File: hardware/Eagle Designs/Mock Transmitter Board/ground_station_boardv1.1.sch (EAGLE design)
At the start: 3 parts, among them J1 MCX-J-P-H-RA-TH1, U1 RFM23BP

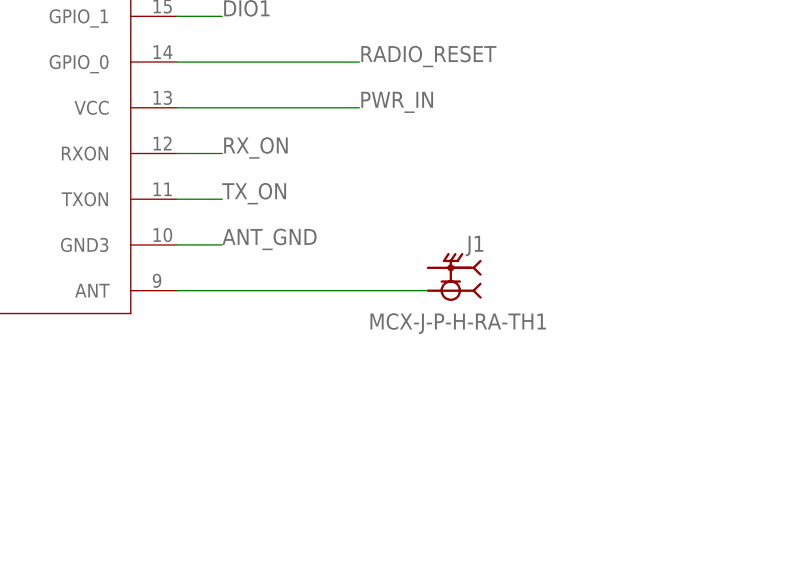
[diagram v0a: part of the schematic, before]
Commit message: Swapped the antenna pad for the MCX connector on the ground station board. Created the mock transmission board which is a radio, teensy and antenna.
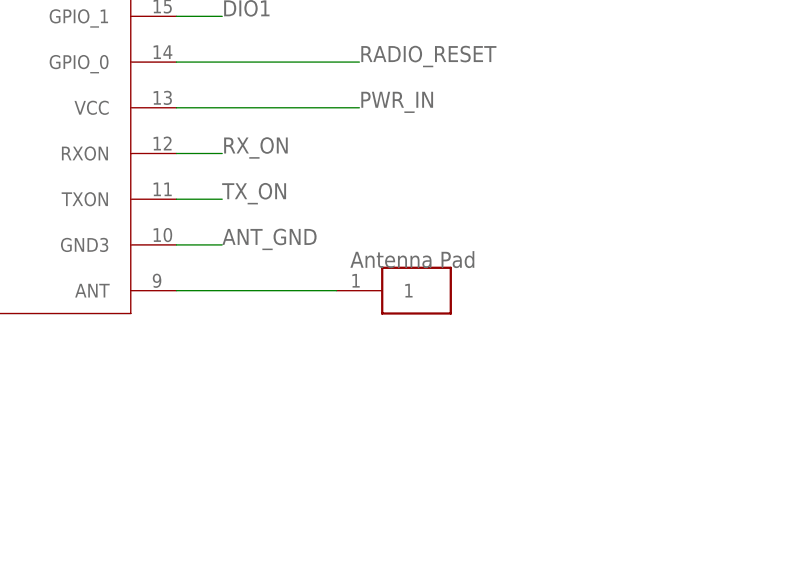
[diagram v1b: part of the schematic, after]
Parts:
- removed J1: MCX-J-P-H-RA-TH1, OBCv4:MCX-J-P-H-RA-TH1
- added U$2: ANTENNA_PAD+HOLES, Antenna_Pad:ANTENNA_PAD+HOLES
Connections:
- net N$1: now also U$2.1; no longer J1.1
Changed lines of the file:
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@@
 <part name="U$1" library="OBCv4" deviceset="TEENSY41" device="TEENSY"/>
 <part name="U1" library="RFM RADIOS" deviceset="RFM23BP" device=""/>
-<part name="J1" library="OBCv4" deviceset="MCX-J-P-H-RA-TH1" device=""/>
+<part name="U$2" library="Antenna_Pad" deviceset="ANTENNA_PAD+HOLES" device=""/>
 </parts>
 <sheets>
@@
 <attribute name="VALUE" x="264.16" y="152.908" size="1.778" layer="96"/>
 </instance>
-<instance part="J1" gate="G$1" x="327.66" y="160.02" smashed="yes" rot="R180">
-<attribute name="NAME" x="331.47" y="163.576" size="1.778" layer="95" rot="R180"/>
-<attribute name="VALUE" x="318.516" y="153.162" size="1.778" layer="96"/>
-</instance>
+<instance part="U$2" gate="G$1" x="320.04" y="154.94" smashed="yes"/>
 </instances>
 <busses>
@@
 <net name="N$1" class="0">
 <segment>
-<pinref part="J1" gate="G$1" pin="1"/>
+<pinref part="U$2" gate="G$1" pin="1"/>
 <pinref part="U1" gate="G$1" pin="ANT"/>
-<wire x1="325.12" y1="157.48" x2="297.18" y2="157.48" width="0.1524" layer="91"/>
-</segment>
-</net>
+<wire x1="314.96" y1="157.48" x2="297.18" y2="157.48" width="0.1524" layer="91"/>
+</segment>
+</net>
